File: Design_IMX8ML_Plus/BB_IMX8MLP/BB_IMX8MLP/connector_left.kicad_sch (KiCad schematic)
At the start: 8 parts, among them J26 DF40C-80DP-0.4V_51_, J31 Front_Right

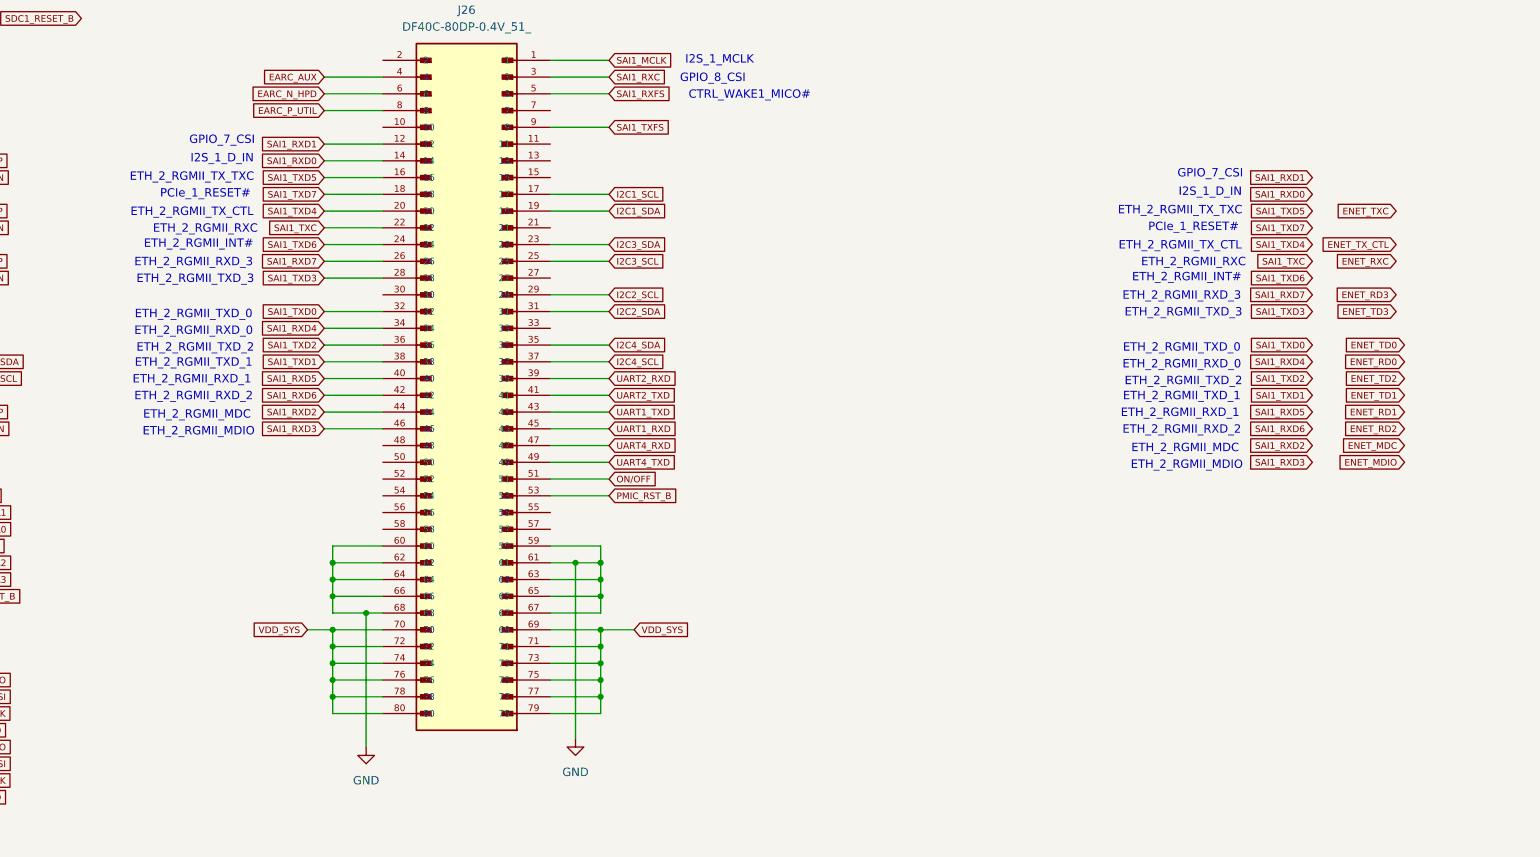
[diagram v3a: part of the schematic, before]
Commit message: [LoRa] Starting a new project
Starting a new project base on LoRa LR1121, this project use
the module LBAA0XV2GT-001 that had sub-GHz and 2.4GHz frequencies.
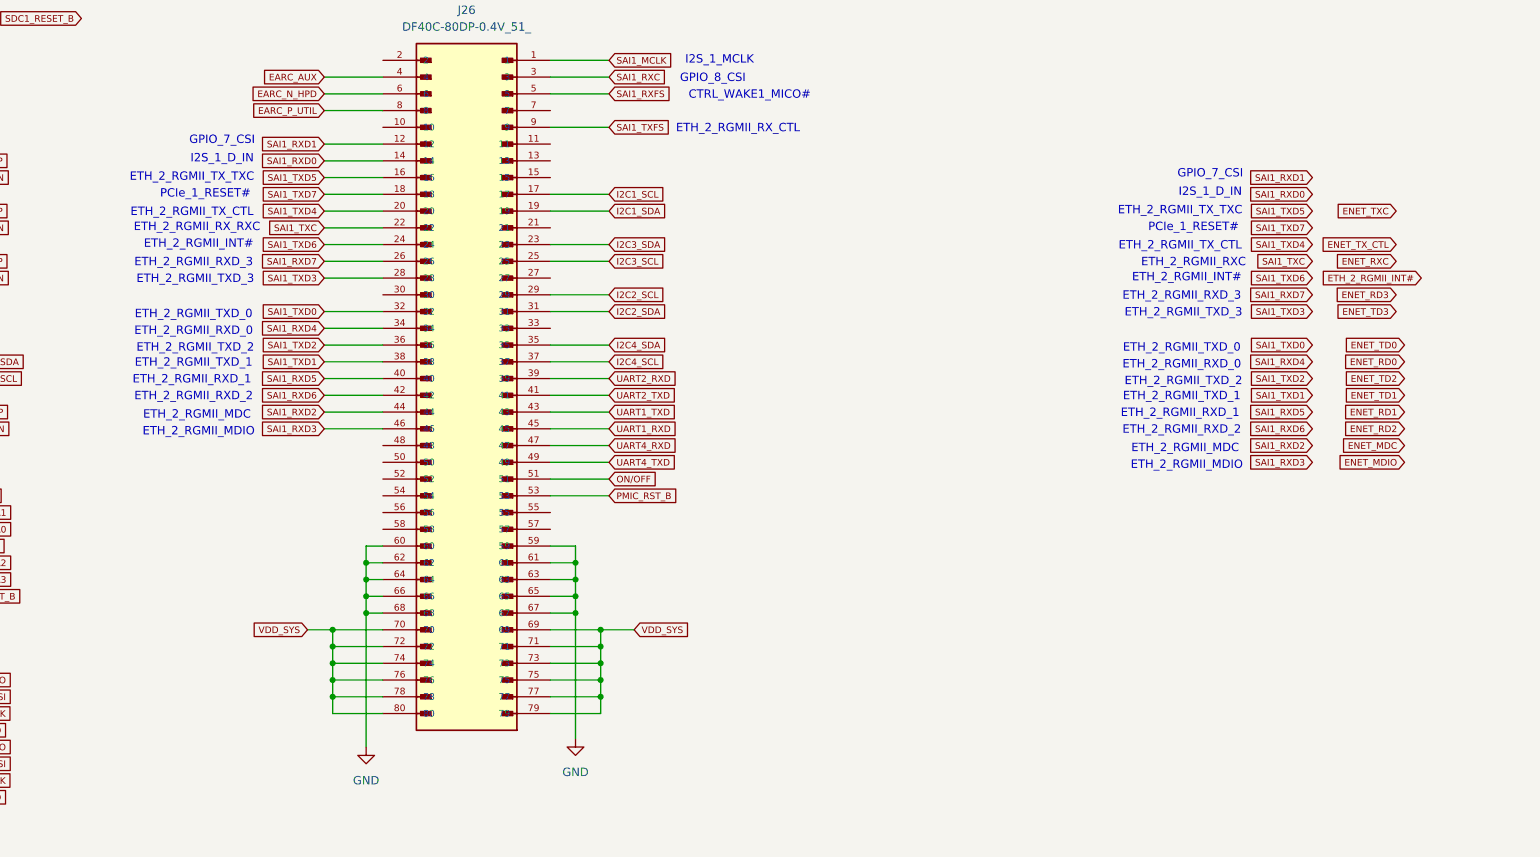
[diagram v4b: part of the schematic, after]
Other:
- note added: "ETH_2_RGMII_RX_CTL"
- note added: "ETH_2_RGMII_RX_RXC"
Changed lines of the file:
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@@
 		)
 	)
+	(text "ETH_2_RGMII_RX_CTL"
+		(exclude_from_sim no)
+		(at 254.508 37.084 0)
+		(effects
+			(font
+				(size 1.27 1.27)
+			)
+		)
+	)
 	(text "ETH_2_RGMII_TXD_1"
 		(exclude_from_sim no)
@@
 		)
 	)
-	(text "ETH_2_RGMII_RXC"
+	(text "ETH_2_RGMII_RX_RXC"
 		(exclude_from_sim no)
-		(at 173.736 52.324 0)
+		(at 172.466 52.07 0)
 		(effects
 			(font
@@
 	)
 	(junction
-		(at 233.68 102.87)
-		(diameter 0)
-		(color 0 0 0 0)
-	)
-	(junction
-		(at 193.04 105.41)
+		(at 198.12 105.41)
 		(diameter 0)
 		(color 0 0 0 0)
@@
 	)
 	(junction
-		(at 193.04 107.95)
+		(at 198.12 107.95)
 		(diameter 0)
 		(color 0 0 0 0)
 	)
 	(junction
-		(at 193.04 102.87)
+		(at 198.12 102.87)
 		(diameter 0)
 		(color 0 0 0 0)
@@
 	)
 	(junction
-		(at 233.68 107.95)
+		(at 229.87 107.95)
 		(diameter 0)
 		(color 0 0 0 0)
@@
 	)
 	(junction
-		(at 233.68 105.41)
+		(at 229.87 105.41)
 		(diameter 0)
 		(color 0 0 0 0)
@@
 	)
 	(junction
+		(at 229.87 110.49)
+		(diameter 0)
+		(color 0 0 0 0)
+	)
+	(junction
 		(at 193.04 115.57)
 		(diameter 0)
@@
 	(wire
 		(pts
-			(xy 193.04 102.87) (xy 200.66 102.87)
+			(xy 198.12 102.87) (xy 200.66 102.87)
 		)
 		(stroke
@@
 	(wire
 		(pts
-			(xy 193.04 110.49) (xy 193.04 107.95)
+			(xy 198.12 110.49) (xy 198.12 107.95)
 		)
 		(stroke
@@
 	(wire
 		(pts
-			(xy 233.68 100.33) (xy 233.68 102.87)
+			(xy 229.87 100.33) (xy 229.87 102.87)
 		)
 		(stroke
@@
 	(wire
 		(pts
-			(xy 193.04 105.41) (xy 193.04 102.87)
+			(xy 198.12 105.41) (xy 198.12 102.87)
 		)
 		(stroke
@@
 	(wire
 		(pts
-			(xy 233.68 102.87) (xy 229.87 102.87)
+			(xy 229.87 102.87) (xy 226.06 102.87)
 		)
 		(stroke
@@
 	(wire
 		(pts
-			(xy 229.87 102.87) (xy 226.06 102.87)
-		)
-		(stroke
-			(width 0)
-			(type default)
-		)
-	)
-	(wire
-		(pts
 			(xy 124.46 80.01) (xy 133.35 80.01)
 		)
@@
 	(wire
 		(pts
-			(xy 193.04 100.33) (xy 193.04 102.87)
+			(xy 198.12 100.33) (xy 198.12 102.87)
 		)
 		(stroke
@@
 	(wire
 		(pts
-			(xy 198.12 110.49) (xy 193.04 110.49)
+			(xy 226.06 26.67) (xy 234.95 26.67)
 		)
 		(stroke
@@
 	(wire
 		(pts
-			(xy 226.06 26.67) (xy 234.95 26.67)
+			(xy 200.66 82.55) (xy 191.77 82.55)
 		)
 		(stroke
@@
 	(wire
 		(pts
-			(xy 200.66 82.55) (xy 191.77 82.55)
+			(xy 229.87 110.49) (xy 229.87 129.54)
 		)
 		(stroke
@@
 	(wire
 		(pts
-			(xy 233.68 110.49) (xy 226.06 110.49)
+			(xy 229.87 110.49) (xy 226.06 110.49)
 		)
 		(stroke
@@
 	(wire
 		(pts
-			(xy 233.68 110.49) (xy 233.68 107.95)
+			(xy 229.87 110.49) (xy 229.87 107.95)
 		)
 		(stroke
@@
 	(wire
 		(pts
-			(xy 200.66 100.33) (xy 193.04 100.33)
+			(xy 200.66 100.33) (xy 198.12 100.33)
 		)
 		(stroke
@@
 	(wire
 		(pts
-			(xy 233.68 107.95) (xy 233.68 105.41)
-		)
-		(stroke
-			(width 0)
-			(type default)
-		)
-	)
-	(wire
-		(pts
 			(xy 99.06 102.87) (xy 90.17 102.87)
 		)
@@
 	(wire
 		(pts
-			(xy 229.87 102.87) (xy 229.87 129.54)
+			(xy 99.06 105.41) (xy 90.17 105.41)
 		)
 		(stroke
@@
 	(wire
 		(pts
-			(xy 99.06 105.41) (xy 90.17 105.41)
+			(xy 124.46 105.41) (xy 133.35 105.41)
 		)
 		(stroke
@@
 	(wire
 		(pts
-			(xy 124.46 105.41) (xy 133.35 105.41)
+			(xy 200.66 41.91) (xy 191.77 41.91)
 		)
 		(stroke
@@
 	(wire
 		(pts
-			(xy 200.66 41.91) (xy 191.77 41.91)
+			(xy 226.06 100.33) (xy 229.87 100.33)
 		)
 		(stroke
@@
 	(wire
 		(pts
-			(xy 226.06 100.33) (xy 233.68 100.33)
+			(xy 229.87 105.41) (xy 229.87 107.95)
 		)
 		(stroke
@@
 	(wire
 		(pts
-			(xy 233.68 105.41) (xy 226.06 105.41)
+			(xy 229.87 105.41) (xy 226.06 105.41)
 		)
 		(stroke
@@
 	(wire
 		(pts
-			(xy 193.04 107.95) (xy 193.04 105.41)
+			(xy 198.12 107.95) (xy 198.12 105.41)
 		)
 		(stroke
@@
 	(wire
 		(pts
-			(xy 233.68 107.95) (xy 226.06 107.95)
+			(xy 229.87 107.95) (xy 226.06 107.95)
 		)
 		(stroke
@@
 	(wire
 		(pts
-			(xy 193.04 107.95) (xy 200.66 107.95)
+			(xy 198.12 107.95) (xy 200.66 107.95)
 		)
 		(stroke
@@
 	(wire
 		(pts
-			(xy 193.04 105.41) (xy 200.66 105.41)
+			(xy 198.12 105.41) (xy 200.66 105.41)
 		)
 		(stroke
@@
 	(wire
 		(pts
-			(xy 233.68 105.41) (xy 233.68 102.87)
+			(xy 229.87 105.41) (xy 229.87 102.87)
 		)
 		(stroke
@@
 				(hide yes)
 			)
+		)
+	)
+	(global_label "ETH_2_RGMII_INT#"
+		(shape input)
+		(at 358.14 59.69 180)
+		(fields_autoplaced yes)
+		(effects
+			(font
+				(size 1 1)
+			)
+			(justify right)
+		)
+		(property "Intersheetrefs" "${INTERSHEET_REFS}"
+			(at 342.4563 59.69 0)
+			(effects
+				(font
+					(size 1.27 1.27)
+				)
+				(justify right)
+				(hide yes)
+			)

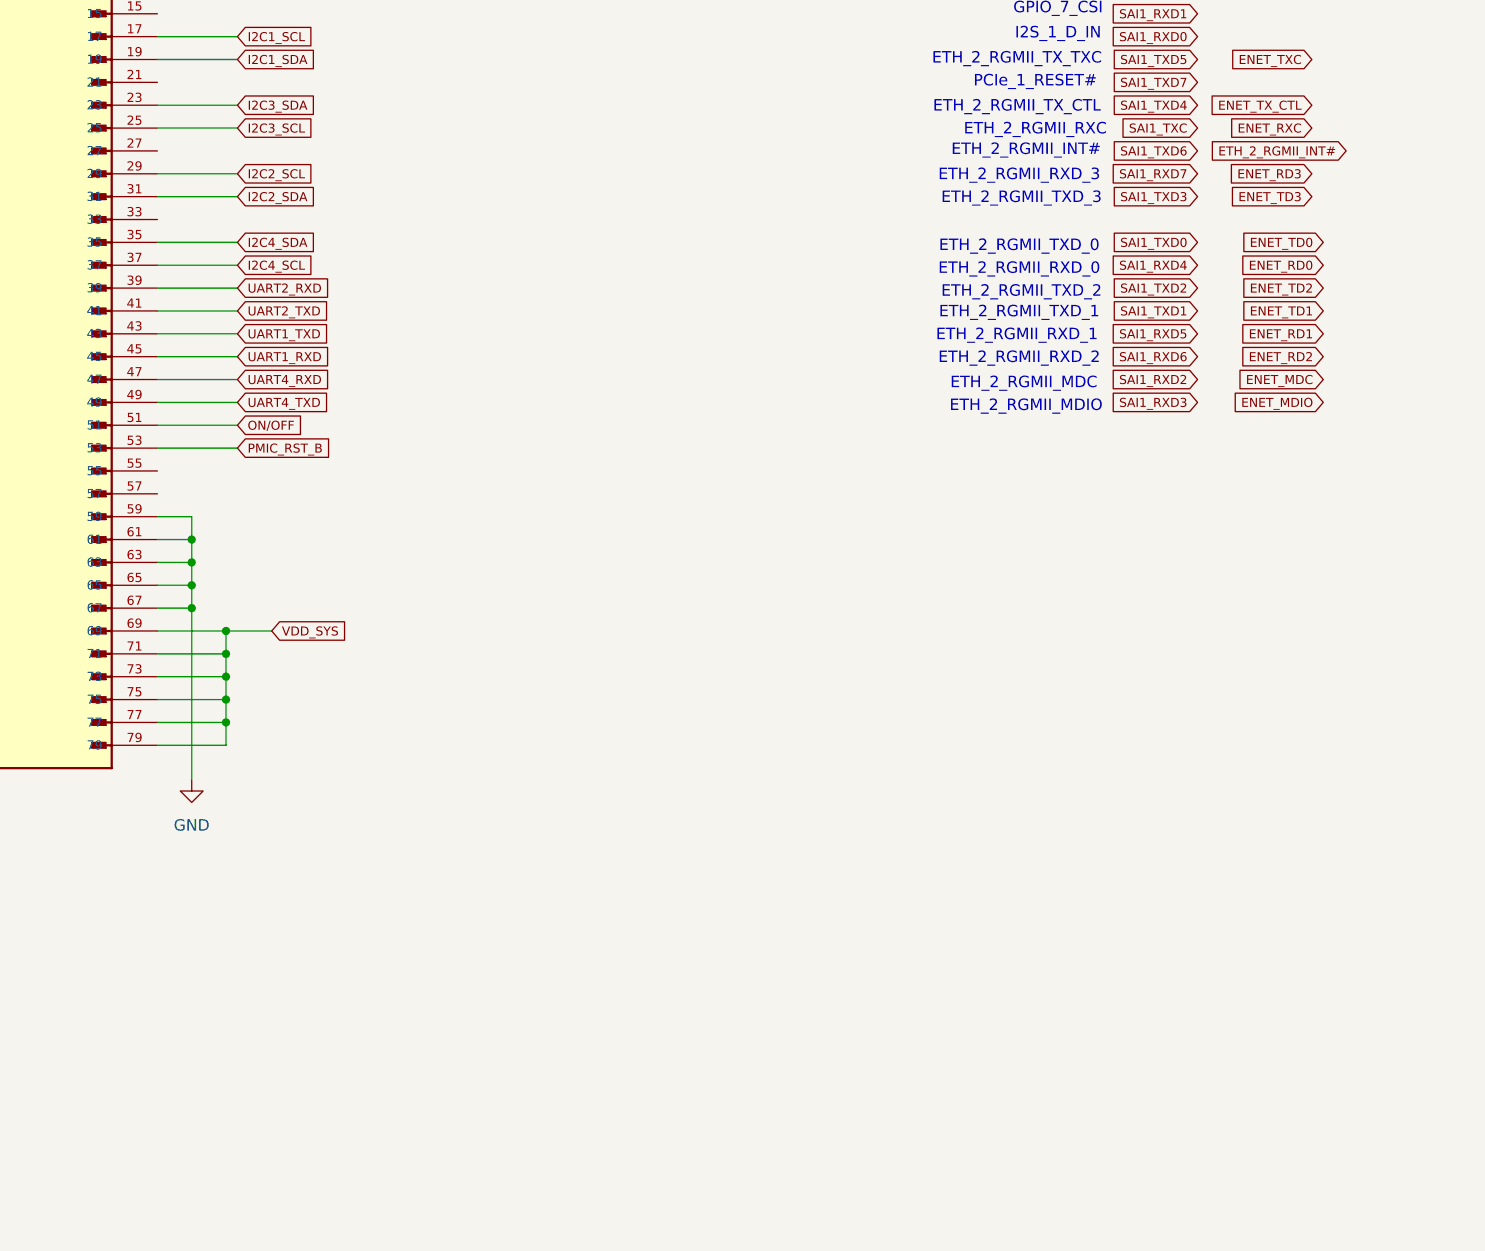
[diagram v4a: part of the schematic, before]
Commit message: [BB_IMX8ML] It was reoganizated the device position
It was reorganized the devices to improve the routing.
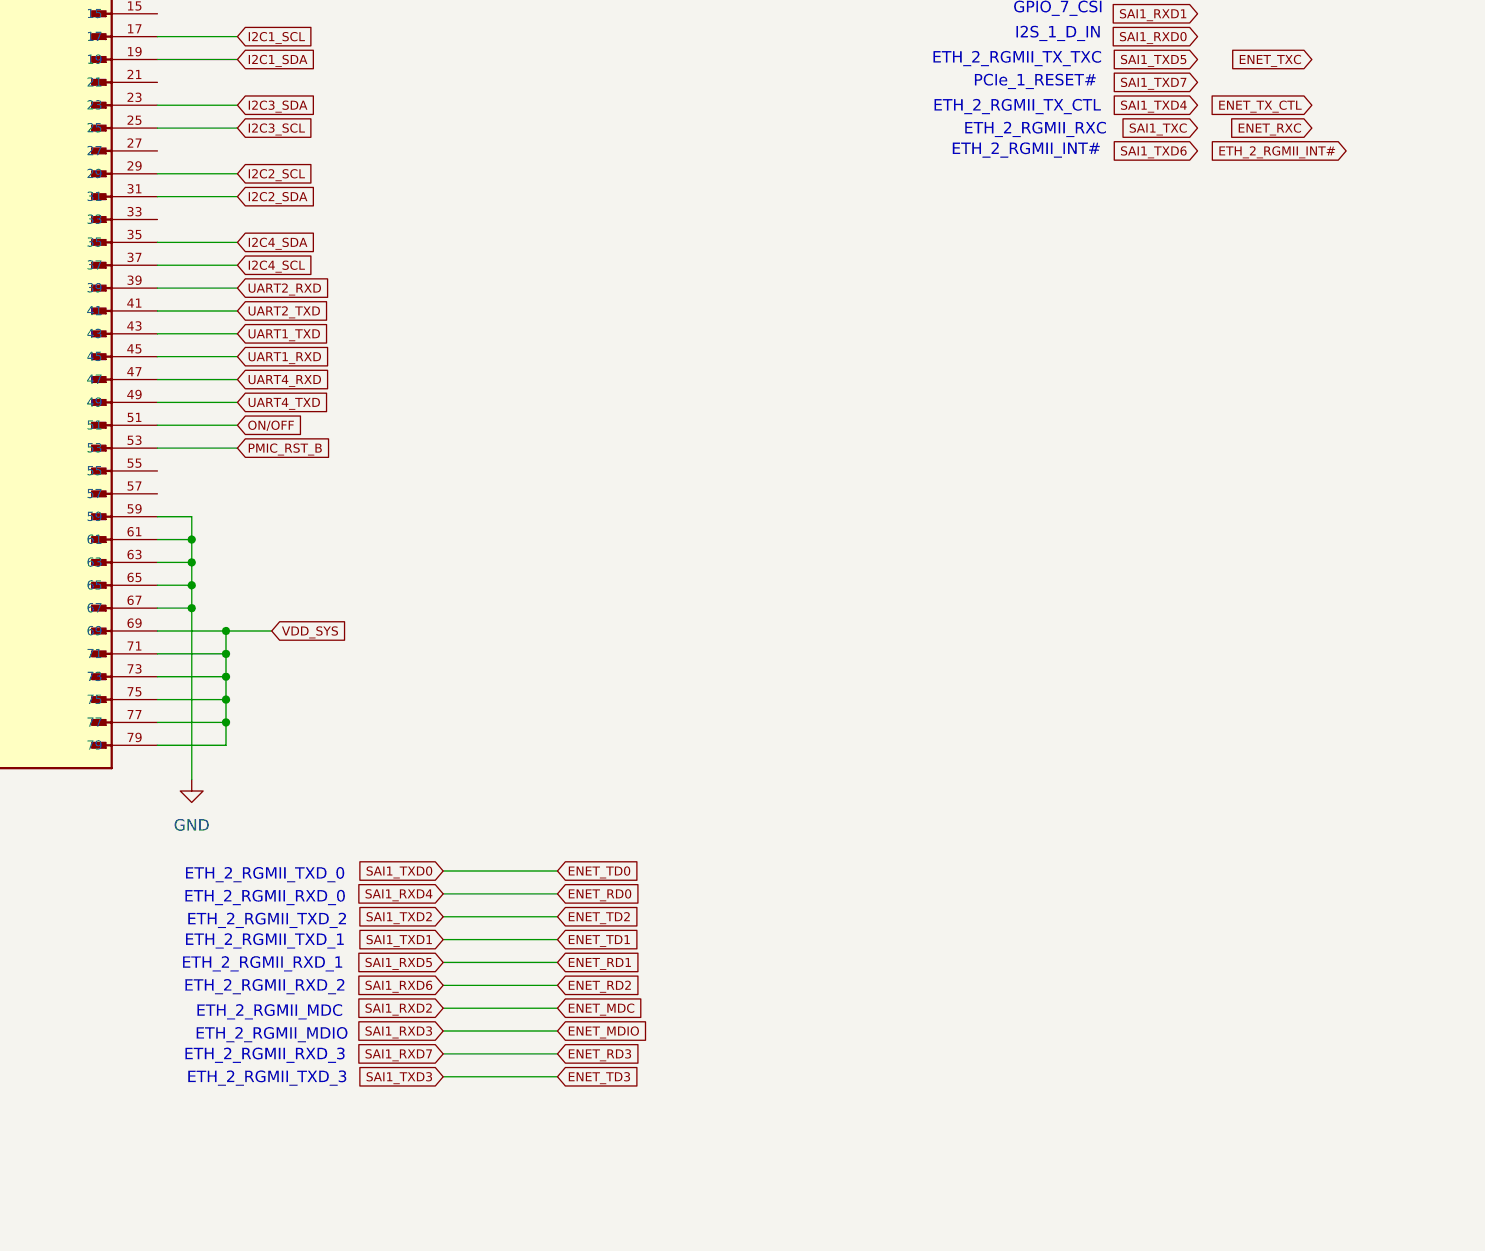
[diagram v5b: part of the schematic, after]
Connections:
- net SAI1_RXD2 is gone; now on net ENET_MDC: J26.44
- net SAI1_RXD3 is gone; now on net ENET_MDIO: J26.46
- net SAI1_RXD4 is gone; now on net ENET_RD0: J26.34
- net SAI1_RXD5 is gone; now on net ENET_RD1: J26.40
- net SAI1_RXD6 is gone; now on net ENET_RD2: J26.42
- net SAI1_RXD7 is gone; now on net ENET_RD3: J26.26
- net SAI1_TXD0 is gone; now on net ENET_TD0: J26.32
- net SAI1_TXD1 is gone; now on net ENET_TD1: J26.38
- net SAI1_TXD2 is gone; now on net ENET_TD2: J26.36
- net SAI1_TXD3 is gone; now on net ENET_TD3: J26.28
